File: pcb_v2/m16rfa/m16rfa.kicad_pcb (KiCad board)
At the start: 2 copper layers, 140.3 x 146.7 mm, 51 parts, among them J1 S16A, J10 bus_rf16_3, J2 S16A, J3 SWRDA, J5 S16A, J6 S16A, J7 S16A, J8 bus_rf16_1, J9 bus_rf16_2, U1 74LS125, U10 74LS244, U11 74LS244, U2 74LS193, U3 74LS138, U4 74LS08, U5 74LS04, U6 74LS08, U7 74LS244, U8 74LS244, U9 74LS244

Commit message: recomeçando o roteamento
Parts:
- moved J9 117.0 mm to (36.8, 39.4), turned to 0 degrees
- moved J8 92.4 mm to (36.8, 69.2), turned to 0 degrees
- moved J10 79.9 mm to (36.8, 99.1), turned to 0 degrees
- moved R8 39.2 mm to (81.9, 63.5)
- moved R9 38.9 mm to (85.7, 63.5)
- moved R10 38.7 mm to (89.5, 63.5)
- moved R11 38.4 mm to (93.3, 63.5)
- moved R12 38.2 mm to (97.2, 63.5)
- moved R15 38.1 mm to (108.6, 63.5)
- moved C8 38.0 mm to (52.7, 46.3)
- moved C9 38.0 mm to (90.2, 46.3)
- moved U8 38.0 mm to (56.5, 48.9)
- moved U9 38.0 mm to (94.0, 48.9)
- moved R13 38.0 mm to (101.0, 63.5)
- moved R16 37.8 mm to (112.4, 63.5)
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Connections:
- J8 pad 11: data_{2} -> data_{5}
- J8 pad 13: data_{1} -> data_{6}
- J8 pad 14: data_{0} -> data_{7}
- J8 pad 3: data_{6} -> data_{1}
- J8 pad 4: data_{7} -> data_{0}
- J8 pad 5: data_{5} -> data_{2}
- J8 pad 7: data_{4} -> data_{3}
- J8 pad 9: data_{3} -> data_{4}
- U4 pad 12: unconnected-(U4-Pad12) -> +5V
- U4 pad 13: unconnected-(U4-Pad13) -> +5V
- U5 pad 11: unconnected-(U5-Pad11) -> +5V
- U5 pad 13: unconnected-(U5-Pad13) -> +5V
- U5 pad 5: unconnected-(U5-Pad5) -> +5V
- U5 pad 9: unconnected-(U5-Pad9) -> +5V
- U6 pad 12: unconnected-(U6-Pad12) -> +5V
- U6 pad 13: unconnected-(U6-Pad13) -> +5V
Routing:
- net +5V: track 582.5 -> 0.00 mm
- net data_{1}: track 130.0 -> 0.00 mm, vias 1 -> 0
- net data_{0}: track 129.7 -> 0.00 mm, vias 1 -> 0
- net data_{2}: track 128.7 -> 0.00 mm, vias 1 -> 0
- net lr_at_two: track 128.4 -> 0.00 mm, vias 2 -> 0
- net data_{3}: track 124.9 -> 0.00 mm, vias 1 -> 0
- net data_{4}: track 122.9 -> 0.00 mm, vias 1 -> 0
- net data_{5}: track 121.2 -> 0.00 mm, vias 1 -> 0
- net data_{6}: track 120.3 -> 0.00 mm
- net lr_at_one: track 118.8 -> 0.00 mm, vias 2 -> 0
- net data_{7}: track 113.3 -> 0.00 mm, vias 1 -> 0
- net lr_at_zero: track 110.8 -> 0.00 mm, vias 2 -> 0
- net addr_{1}: track 102.4 -> 0.00 mm, vias 1 -> 0
- net addr_{3}: track 100.7 -> 0.00 mm, vias 1 -> 0
- net addr_{0}: track 100.6 -> 0.00 mm, vias 1 -> 0
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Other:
- board size 140.3 x 146.7 mm -> 146.7 x 134 mm

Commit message: .
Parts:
- moved J1 13.3 mm to (79.4, 78.7)
- moved J2 12.7 mm to (66.0, 78.7)
- moved J10 8.89 mm to (36.8, 108.0)
- moved J8 8.89 mm to (36.8, 78.1)
- moved J9 8.89 mm to (36.8, 48.3)
- moved J3 0.32 mm to (52.7, 78.7)
- moved J5 0.32 mm to (92.1, 78.7)
- moved J6 0.32 mm to (105.4, 78.7)
- moved J7 0.32 mm to (118.7, 78.7)
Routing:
- net addr_{6}: track 0.00 -> 89.2 mm
- net addr_{2}: track 0.00 -> 89.2 mm
- net addr_{8}: track 0.00 -> 89.2 mm
- net addr_{14}: track 0.00 -> 89.2 mm
- net addr_{12}: track 0.00 -> 89.2 mm
- net addr_{0}: track 0.00 -> 89.2 mm
- net addr_{4}: track 0.00 -> 89.2 mm
- net addr_{10}: track 0.00 -> 89.2 mm
- net addr_{9}: track 0.00 -> 87.7 mm, vias 0 -> 2
- net addr_{15}: track 0.00 -> 87.7 mm, vias 0 -> 2
- net addr_{13}: track 0.00 -> 87.7 mm, vias 0 -> 2
- net addr_{7}: track 0.00 -> 87.7 mm, vias 0 -> 2
- net addr_{3}: track 0.00 -> 87.7 mm, vias 0 -> 2
- net addr_{5}: track 0.00 -> 87.7 mm, vias 0 -> 2
- net addr_{11}: track 0.00 -> 87.7 mm, vias 0 -> 2
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
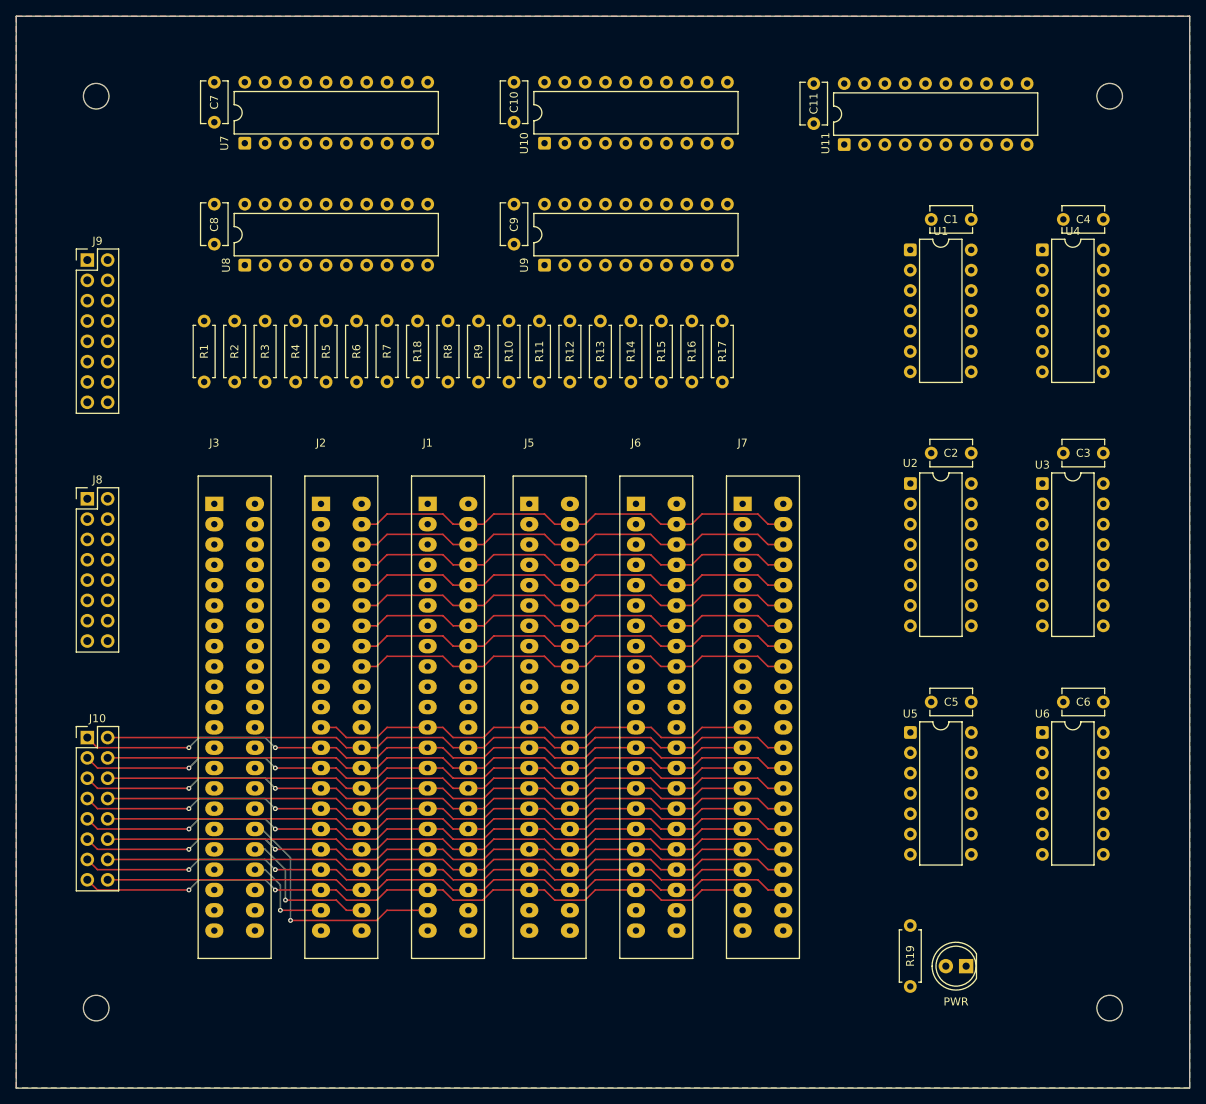
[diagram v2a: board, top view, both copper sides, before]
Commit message: concluído o roteamento; falta corrigir os erros apontados pela validação de regras
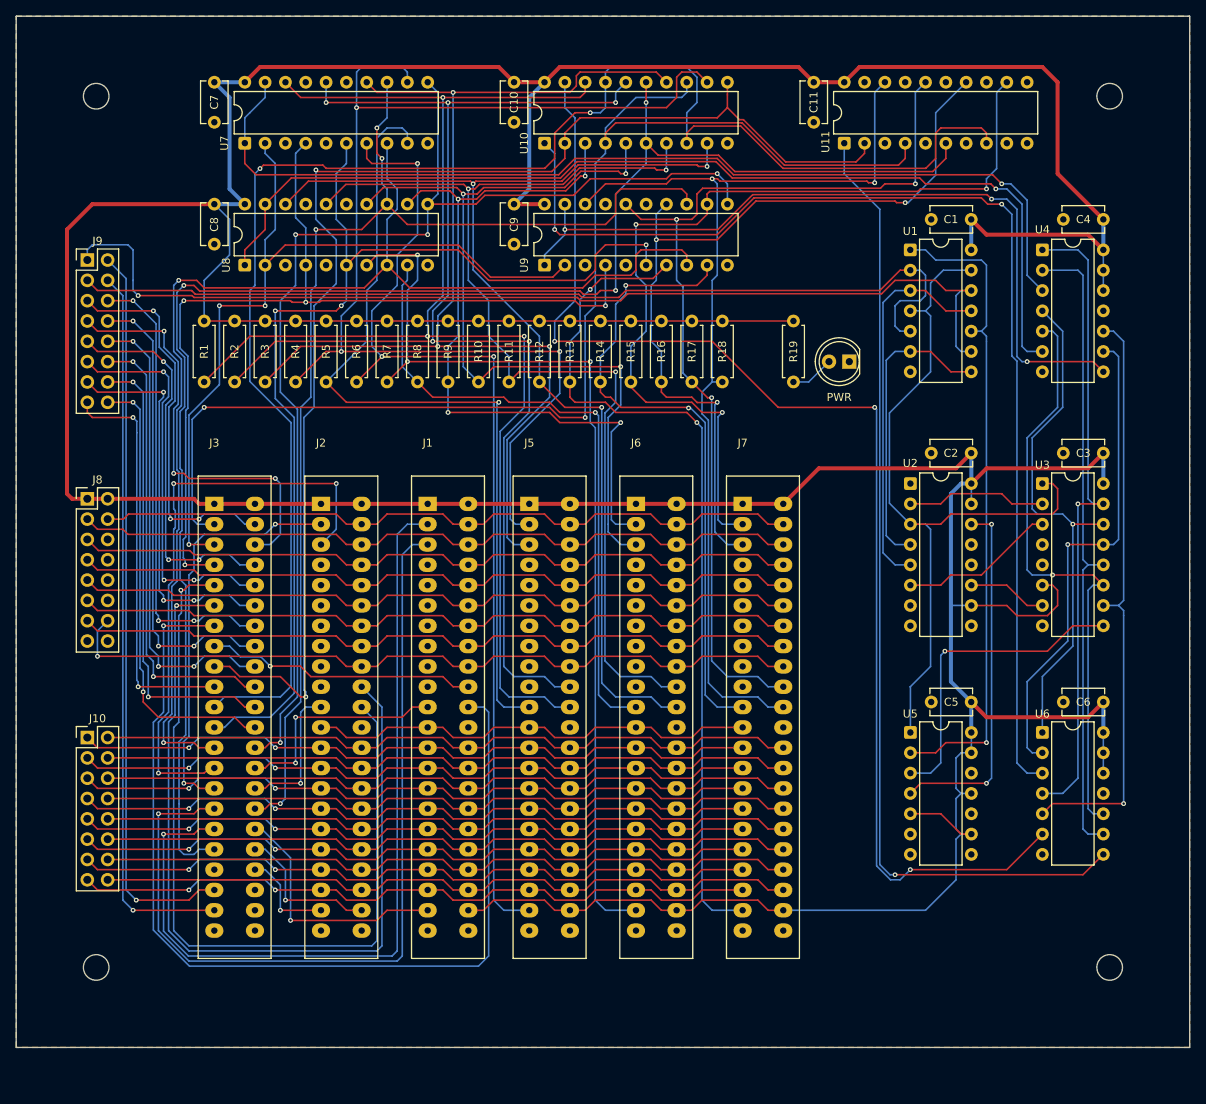
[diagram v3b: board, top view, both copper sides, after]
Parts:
- moved D1 77.0 mm to (132.1, 61.0)
- moved R19 77.0 mm to (125.1, 63.5)
- moved R18 38.9 mm to (116.2, 55.9), turned to -90 degrees
- moved R10 8.52 mm to (85.7, 55.9), turned to -90 degrees
- moved R11 8.52 mm to (89.5, 55.9), turned to -90 degrees
- moved R12 8.52 mm to (93.3, 55.9), turned to -90 degrees
- moved R13 8.52 mm to (97.2, 55.9), turned to -90 degrees
- moved R14 8.52 mm to (101.0, 55.9), turned to -90 degrees
- moved R16 8.52 mm to (108.6, 55.9), turned to -90 degrees
- moved R17 8.52 mm to (112.4, 55.9), turned to -90 degrees
- moved R8 8.52 mm to (78.1, 55.9), turned to -90 degrees
- moved R15 8.52 mm to (104.8, 55.9), turned to -90 degrees
- moved R9 8.52 mm to (81.9, 55.9), turned to -90 degrees
- moved R1 7.62 mm to (51.4, 55.9), turned to -90 degrees
- moved R2 7.62 mm to (55.2, 55.9), turned to -90 degrees
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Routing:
- net +5V: track 0.00 -> 666.6 mm
- net ~{read_lrl}: track 0.00 -> 201.0 mm, vias 0 -> 3
- net ~{read_lrh}: track 0.00 -> 198.8 mm, vias 0 -> 2
- net ~{write_zero_l}: track 0.00 -> 167.7 mm, vias 0 -> 3
- net ~{write_lrl}: track 0.00 -> 163.2 mm, vias 0 -> 2
- net ~{write_zero_h}: track 0.00 -> 162.6 mm, vias 0 -> 5
- net ~{write_lrh}: track 0.00 -> 160.0 mm, vias 0 -> 2
- net lr_at_one: track 0.00 -> 158.6 mm, vias 0 -> 3
- net ~{read_pch}: track 0.00 -> 153.3 mm, vias 0 -> 2
- net ~{read_zero_h}: track 0.00 -> 152.3 mm, vias 0 -> 3
- net ~{addr_pc}: track 0.00 -> 148.2 mm, vias 0 -> 4
- net pc_inc: track 0.00 -> 146.9 mm, vias 0 -> 4
- net lr_at_zero: track 0.00 -> 144.0 mm, vias 0 -> 2
- net ~{write_one_l}: track 0.00 -> 140.4 mm, vias 0 -> 3
- net ~{read_zero_l}: track 0.00 -> 139.5 mm, vias 0 -> 3
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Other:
- board size 146.7 x 134 mm -> 146.7 x 128.9 mm

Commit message: .
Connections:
- J9 pad 1: pclr_swap -> ~{pclr_swap}
- J9 pad 3: pcia_swap -> ~{pcia_swap}
- U5 pad 10: unconnected-(U5-Pad10) -> pclr_swap
- U5 pad 11: +5V -> ~{pcia_swap}
- U5 pad 8: unconnected-(U5-Pad8) -> pcia_swap
- U5 pad 9: +5V -> ~{pclr_swap}
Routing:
- net ~{pclr_swap}: track 0.00 -> 191.8 mm, vias 0 -> 1
- net ~{pcia_swap}: track 0.00 -> 182.8 mm, vias 0 -> 1
- net pclr_swap: track 130.2 -> 76.9 mm, vias 1 -> 2
- net pcia_swap: track 118.9 -> 92.6 mm, vias 0 -> 1
- net +5V: track 666.6 -> 652.5 mm
- net lr_at_one: track 158.6 -> 148.9 mm
- net lr_at_two: track 121.5 -> 113.5 mm
- net ~{read_pcl}: track 136.0 -> 130.9 mm, vias 3 -> 2
- net ~{write_spl}: track 103.9 -> 106.8 mm
- net inc_one: track 120.4 -> 117.7 mm, vias 3 -> 4
- net ~{addr_pc}: track 148.2 -> 145.6 mm
- net pc_inc: track 146.9 -> 144.4 mm, vias 4 -> 5
- net data_{7}: track 95.4 -> 93.1 mm
- net pc_at_one: track 128.3 -> 130.5 mm, vias 1 -> 2
- net ~{write_sph}: track 107.2 -> 109.3 mm
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
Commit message: refazendo o módulo de registradores
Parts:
- removed J3: SWRDA, edge_connector:male-edge-connector-44
- added C12: 100nF, Capacitor_THT:C_Disc_D5.1mm_W3.2mm_P5.00mm, F.Cu at (248.6, 93.1)
- added C13: 100nF, Capacitor_THT:C_Disc_D5.1mm_W3.2mm_P5.00mm, F.Cu at (248.6, 97.8)
- added C14: 100nF, Capacitor_THT:C_Disc_D5.1mm_W3.2mm_P5.00mm, F.Cu at (248.6, 102.6)
- added C15: 100nF, Capacitor_THT:C_Disc_D5.1mm_W3.2mm_P5.00mm, F.Cu at (248.6, 107.3)
- added C16: 100nF, Capacitor_THT:C_Disc_D5.1mm_W3.2mm_P5.00mm, F.Cu at (248.6, 112.1)
- added C17: 100nF, Capacitor_THT:C_Disc_D5.1mm_W3.2mm_P5.00mm, F.Cu at (248.6, 116.8)
- added C18: 100nF, Capacitor_THT:C_Disc_D5.1mm_W3.2mm_P5.00mm, F.Cu at (248.6, 121.6)
- added C19: 100nF, Capacitor_THT:C_Disc_D5.1mm_W3.2mm_P5.00mm, F.Cu at (256.7, 93.1)
- added C20: 100nF, Capacitor_THT:C_Disc_D5.1mm_W3.2mm_P5.00mm, F.Cu at (256.7, 97.8)
- added C21: 100nF, Capacitor_THT:C_Disc_D5.1mm_W3.2mm_P5.00mm, F.Cu at (256.7, 102.6)
- added C22: 100nF, Capacitor_THT:C_Disc_D5.1mm_W3.2mm_P5.00mm, F.Cu at (256.7, 107.3)
- added C23: 100nF, Capacitor_THT:C_Disc_D5.1mm_W3.2mm_P5.00mm, F.Cu at (256.7, 112.1)
- added C24: 100nF, Capacitor_THT:C_Disc_D5.1mm_W3.2mm_P5.00mm, F.Cu at (256.7, 116.8)
- added C25: 100nF, Capacitor_THT:C_Disc_D5.1mm_W3.2mm_P5.00mm, F.Cu at (256.7, 121.6)
- added C26: 100nF, Capacitor_THT:C_Disc_D5.1mm_W3.2mm_P5.00mm, F.Cu at (264.9, 93.1)
- added C27: 100nF, Capacitor_THT:C_Disc_D5.1mm_W3.2mm_P5.00mm, F.Cu at (264.9, 97.8)
- added C28: 100nF, Capacitor_THT:C_Disc_D5.1mm_W3.2mm_P5.00mm, F.Cu at (264.9, 102.6)
- added C29: 100nF, Capacitor_THT:C_Disc_D5.1mm_W3.2mm_P5.00mm, F.Cu at (264.9, 107.3)
- added D10: RD, LED_THT:LED_D5.0mm, F.Cu at (234.5, 116.8)
- added D11: WR, LED_THT:LED_D5.0mm, F.Cu at (234.5, 124.3)
- added D12: RD, LED_THT:LED_D5.0mm, F.Cu at (242.0, 94.4)
- added D13: WR, LED_THT:LED_D5.0mm, F.Cu at (242.0, 101.9)
- added D14: RD, LED_THT:LED_D5.0mm, F.Cu at (242.0, 109.4)
- added D15: WR, LED_THT:LED_D5.0mm, F.Cu at (242.0, 116.8)
- added D2: RD, LED_THT:LED_D5.0mm, F.Cu at (227.0, 94.4)
- added D3: WR, LED_THT:LED_D5.0mm, F.Cu at (227.0, 101.9)
- added D4: RD, LED_THT:LED_D5.0mm, F.Cu at (227.0, 109.4)
- added D5: WR, LED_THT:LED_D5.0mm, F.Cu at (227.0, 116.8)
- added D6: RD, LED_THT:LED_D5.0mm, F.Cu at (227.0, 124.3)
- added D7: WR, LED_THT:LED_D5.0mm, F.Cu at (234.5, 94.4)
- added D8: RD, LED_THT:LED_D5.0mm, F.Cu at (234.5, 101.9)
- added D9: WR, LED_THT:LED_D5.0mm, F.Cu at (234.5, 109.4)
- added R20: 1K, Resistor_THT:R_Axial_DIN0207_L6.3mm_D2.5mm_P7.62mm_Horizontal, F.Cu at (215.4, 73.4)
- added R21: 1K, Resistor_THT:R_Axial_DIN0207_L6.3mm_D2.5mm_P7.62mm_Horizontal, F.Cu at (215.4, 77.4)
- added R22: 1K, Resistor_THT:R_Axial_DIN0207_L6.3mm_D2.5mm_P7.62mm_Horizontal, F.Cu at (215.4, 81.5)
- added R23: 1K, Resistor_THT:R_Axial_DIN0207_L6.3mm_D2.5mm_P7.62mm_Horizontal, F.Cu at (215.4, 85.5)
- added R25: 1K, Resistor_THT:R_Axial_DIN0207_L6.3mm_D2.5mm_P7.62mm_Horizontal, F.Cu at (215.4, 89.6)
- added R26: 1K, Resistor_THT:R_Axial_DIN0207_L6.3mm_D2.5mm_P7.62mm_Horizontal, F.Cu at (215.4, 93.6)
- added R27: 1K, Resistor_THT:R_Axial_DIN0207_L6.3mm_D2.5mm_P7.62mm_Horizontal, F.Cu at (215.4, 97.7)
- added R28: 1K, Resistor_THT:R_Axial_DIN0207_L6.3mm_D2.5mm_P7.62mm_Horizontal, F.Cu at (215.4, 101.7)
- added R29: 1K, Resistor_THT:R_Axial_DIN0207_L6.3mm_D2.5mm_P7.62mm_Horizontal, F.Cu at (215.4, 105.8)
- added R30: 1K, Resistor_THT:R_Axial_DIN0207_L6.3mm_D2.5mm_P7.62mm_Horizontal, F.Cu at (215.4, 109.8)
- added R31: 1K, Resistor_THT:R_Axial_DIN0207_L6.3mm_D2.5mm_P7.62mm_Horizontal, F.Cu at (215.4, 113.9)
- added R32: 1K, Resistor_THT:R_Axial_DIN0207_L6.3mm_D2.5mm_P7.62mm_Horizontal, F.Cu at (215.4, 117.9)
- added R33: 1K, Resistor_THT:R_Axial_DIN0207_L6.3mm_D2.5mm_P7.62mm_Horizontal, F.Cu at (215.4, 122.0)
- added R34: 1K, Resistor_THT:R_Axial_DIN0207_L6.3mm_D2.5mm_P7.62mm_Horizontal, F.Cu at (215.4, 126.0)
- added U12: 74LS574, Package_DIP:DIP-20_W7.62mm, F.Cu at (110.5, 113.0)
- added U13: 74LS02, Package_DIP:DIP-14_W7.62mm, F.Cu at (226.1, 73.4)
- added U14: 74LS04, Package_DIP:DIP-14_W7.62mm, F.Cu at (236.9, 73.4)
- added U15: 74LS574, Package_DIP:DIP-20_W7.62mm, F.Cu at (121.3, 113.0)
- added U16: 74LS574, Package_DIP:DIP-20_W7.62mm, F.Cu at (132.1, 113.0)
- added U17: 74LS574, Package_DIP:DIP-20_W7.62mm, F.Cu at (142.9, 113.0)
- added U18: 74LS574, Package_DIP:DIP-20_W7.62mm, F.Cu at (109.9, 74.9)
- added U19: 74LS574, Package_DIP:DIP-20_W7.62mm, F.Cu at (120.7, 74.9)
- added U20: 74LS574, Package_DIP:DIP-20_W7.62mm, F.Cu at (131.4, 74.9)
- added U21: 74LS08, Package_DIP:DIP-14_W7.62mm, F.Cu at (247.7, 73.4)
- added U22: 74LS138, Package_DIP:DIP-16_W7.62mm, F.Cu at (132.1, 45.1)
- added U23: 74LS138, Package_DIP:DIP-16_W7.62mm, F.Cu at (142.9, 45.1)
- added U24: 74LS32, Package_DIP:DIP-14_W7.62mm, F.Cu at (258.5, 73.4)
- added U25: 74LS00, Package_DIP:DIP-14_W7.62mm, F.Cu at (269.3, 73.4)
- added U26: 74LS138, Package_DIP:DIP-16_W7.62mm, F.Cu at (236.9, 51.5)
- added U27: 74LS138, Package_DIP:DIP-16_W7.62mm, F.Cu at (247.7, 51.5)
- added U28: 74LS138, Package_DIP:DIP-16_W7.62mm, F.Cu at (258.5, 51.5)
- added U29: 74LS138, Package_DIP:DIP-16_W7.62mm, F.Cu at (269.3, 51.5)
- moved J9 148.8 mm to (168.9, 116.8), turned to 90 degrees
- moved J8 141.1 mm to (168.9, 127.6), turned to 90 degrees
- moved J10 135.4 mm to (168.9, 137.8), turned to 90 degrees
- moved C1 31.0 mm to (167.7, 25.4)
- moved C2 31.0 mm to (167.7, 54.6)
- moved C5 31.0 mm to (167.7, 85.7)
- moved U1 31.0 mm to (165.1, 29.2)
- moved U2 31.0 mm to (165.1, 58.4)
- moved U3 31.0 mm to (181.6, 58.4)
- moved U4 31.0 mm to (181.6, 29.2)
- moved U5 31.0 mm to (165.1, 89.5)
- moved U6 31.0 mm to (181.6, 89.5)
- moved C3 31.0 mm to (184.2, 54.6)
- moved C4 31.0 mm to (184.2, 25.4)
- moved C6 31.0 mm to (184.2, 85.7)
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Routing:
- net +5V: track 652.5 -> 0.00 mm
- net ~{read_lrl}: track 201.0 -> 0.00 mm, vias 3 -> 0
- net ~{read_lrh}: track 198.8 -> 0.00 mm, vias 2 -> 0
- net ~{pclr_swap}: track 191.8 -> 0.00 mm, vias 1 -> 0
- net ~{pcia_swap}: track 182.8 -> 0.00 mm, vias 1 -> 0
- net ~{write_zero_l}: track 167.7 -> 0.00 mm, vias 3 -> 0
- net ~{write_lrl}: track 163.2 -> 0.00 mm, vias 2 -> 0
- net ~{write_zero_h}: track 162.6 -> 0.00 mm, vias 5 -> 0
- net ~{write_lrh}: track 160.0 -> 0.00 mm, vias 2 -> 0
- net ~{read_zero_h}: track 152.3 -> 0.00 mm, vias 3 -> 0
- net ~{read_pch}: track 151.4 -> 0.00 mm, vias 3 -> 0
- net lr_at_one: track 148.9 -> 0.00 mm, vias 3 -> 0
- net ~{addr_pc}: track 145.6 -> 0.00 mm, vias 4 -> 0
- net lr_at_zero: track 144.9 -> 0.00 mm, vias 2 -> 0
- net pc_inc: track 144.4 -> 0.00 mm, vias 5 -> 0
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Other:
- board size 146.7 x 128.9 mm -> 172.7 x 125.1 mm

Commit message: Redimensionamento do clock para abrir mais espaço para os registradores
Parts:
- removed C12, C15, C16, C17, C18, C19, C20: 100nF, Capacitor_THT:C_Disc_D5.1mm_W3.2mm_P5.00mm
- removed D10, D12, D14, D2, D4, D6, D8: RD, LED_THT:LED_D5.0mm
- removed D11, D13, D3, D5, D7, D9: WR, LED_THT:LED_D5.0mm
- removed the D15 at (242.0, 116.8)
- removed R20, R21, R22, R23, R25, R26, R27, R28, R29, R30, R31, R32, R33, R34: 1K, Resistor_THT:R_Axial_DIN0207_L6.3mm_D2.5mm_P7.62mm_Horizontal
- removed U12, U15, U16, U17, U18, U19, U20: 74LS574, Package_DIP:DIP-20_W7.62mm
- added J3: SR8A, edge_connector:male-edge-connector-44, F.Cu at (103.5, 81.3)
- moved C29 235.0 mm to (43.9, 27.3)
- moved U29 228.9 mm to (41.3, 31.1)
- moved C26 200.3 mm to (75.6, 27.3)
- moved C22 182.5 mm to (92.7, 27.3)
- moved U26 165.2 mm to (73.0, 31.1)
- moved C23 153.8 mm to (126.4, 30.4), turned to 90 degrees
- moved U25 143.7 mm to (128.3, 101.0), turned to 90 degrees
- moved C24 140.4 mm to (126.4, 64.7), turned to 90 degrees
- moved C25 134.3 mm to (124.5, 98.3), turned to 90 degrees
- moved C13 133.8 mm to (125.1, 46.3), turned to 90 degrees
- moved U24 128.5 mm to (130.2, 67.3), turned to 90 degrees
- moved C9 123.5 mm to (165.1, 133.9)
- moved U9 123.5 mm to (168.9, 136.5)
- moved C10 122.1 mm to (165.1, 116.8)
- moved U10 122.1 mm to (168.9, 119.4)
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- renumbered D1 to D15
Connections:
- U13 pad 11: unconnected-(U13-Pad11) -> +5V
- U13 pad 12: unconnected-(U13-Pad12) -> +5V
- U13 pad 8: unconnected-(U13-Pad8) -> +5V
- U13 pad 9: unconnected-(U13-Pad9) -> +5V
- U22 pad 10: ~{sel_write_marh} -> ~{write_marh}
- U22 pad 11: ~{sel_write_marl} -> ~{write_marl}
- U22 pad 12: ~{sel_write_sph} -> ~{write_sph}
- U22 pad 13: ~{sel_write_spl} -> ~{write_spl}
- U22 pad 14: ~{sel_write_pch} -> ~{write_pch}
- U22 pad 15: ~{sel_write_pcl} -> ~{write_pcl}
- U22 pad 7: ~{sel_write_lrh} -> ~{write_lrh}
- U22 pad 9: ~{sel_write_lrl} -> ~{write_lrl}
- U24 pad 10: unconnected-(U24-Pad10) -> +5V
- U24 pad 12: unconnected-(U24-Pad12) -> +5V
- U24 pad 13: unconnected-(U24-Pad13) -> +5V
- U24 pad 9: unconnected-(U24-Pad9) -> +5V
- U26 pad 10: ~{sel_read_marh} -> ~{read_marh}
- U26 pad 11: ~{sel_read_marl} -> ~{read_marl}
- U26 pad 12: ~{sel_read_sph} -> ~{read_sph}
- U26 pad 13: ~{sel_read_spl} -> ~{read_spl}
- U26 pad 14: ~{sel_read_pch} -> ~{read_pch}
- U26 pad 15: ~{sel_read_pcl} -> ~{read_pcl}
- U26 pad 7: ~{sel_read_lrh} -> ~{read_lrh}
- U26 pad 9: ~{sel_read_lrl} -> ~{read_lrl}
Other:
- board size 172.7 x 125.1 mm -> 209.5 x 125.1 mm

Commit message: revisão na posição dos conectores
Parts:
- moved J10 10.2 mm to (210.8, 118.1)
- moved J8 10.2 mm to (210.8, 128.3)
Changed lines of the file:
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@@
 	(footprint "Connector_PinHeader_2.54mm:PinHeader_2x08_P2.54mm_Vertical"
 		(layer "F.Cu")
-		(at 210.79 118.11 90)
+		(at 210.79 128.27 90)
 		(descr "Through hole straight pin header, 2x08, 2.54mm pitch, double rows")
 		(tags "Through hole pin header THT 2x08 2.54mm double row")
@@
 	(footprint "Connector_PinHeader_2.54mm:PinHeader_2x08_P2.54mm_Vertical"
 		(layer "F.Cu")
-		(at 210.79 128.27 90)
+		(at 210.82 118.11 90)
 		(descr "Through hole straight pin header, 2x08, 2.54mm pitch, double rows")
 		(tags "Through hole pin header THT 2x08 2.54mm double row")
@@
 	)
 	(gr_rect
-		(start 205.68 103.045)
-		(end 233.68 109.045)
+		(start 205.68 113.84)
+		(end 233.68 119.84)
 		(stroke
 			(width 0.1)
@@
 	)
 	(gr_rect
-		(start 205.68 113.84)
-		(end 233.68 119.84)
+		(start 205.68 103.045)
+		(end 233.68 109.045)
 		(stroke
 			(width 0.1)
@@
 	)
 	(gr_circle
+		(center 231.485 137.51)
+		(end 233.085 137.51)
+		(stroke
+			(width 0.05)
+			(type solid)
+		)
+		(fill no)
+		(layer "Edge.Cuts")
+	)
+	(gr_circle
 		(center 33.94 24.415)
 		(end 35.54 24.415)
@@
 		(stroke
 			(width 0.05)
-			(type solid)
-		)
-		(fill no)
-		(layer "Edge.Cuts")
-	)
-	(gr_circle
-		(center 231.485 137.51)
-		(end 233.085 137.51)
-		(stroke
-			(width 0.05)
